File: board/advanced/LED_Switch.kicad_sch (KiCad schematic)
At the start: 14 parts, among them J11 LED, J12 LED, Q2 2SC4213, Q3 2SC4213, SW3 SW_{R}, SW4 SW_{L}, SW5 SW_DIP_x04

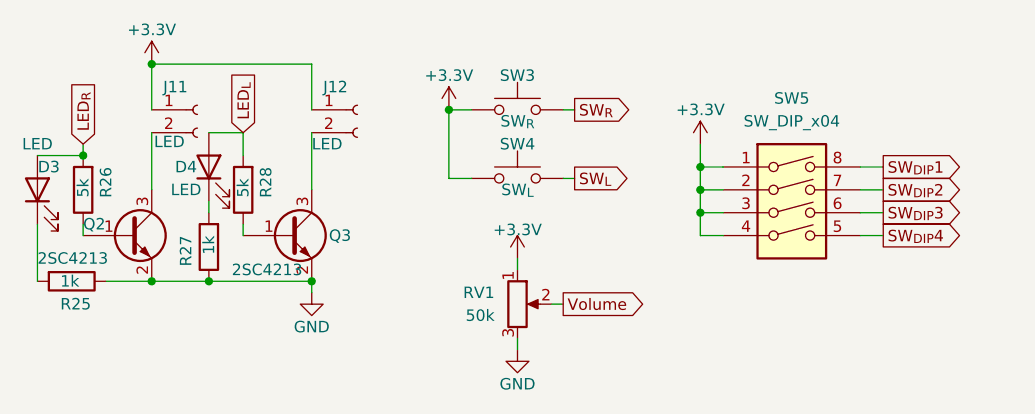
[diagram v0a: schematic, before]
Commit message: put footprints and change schematics
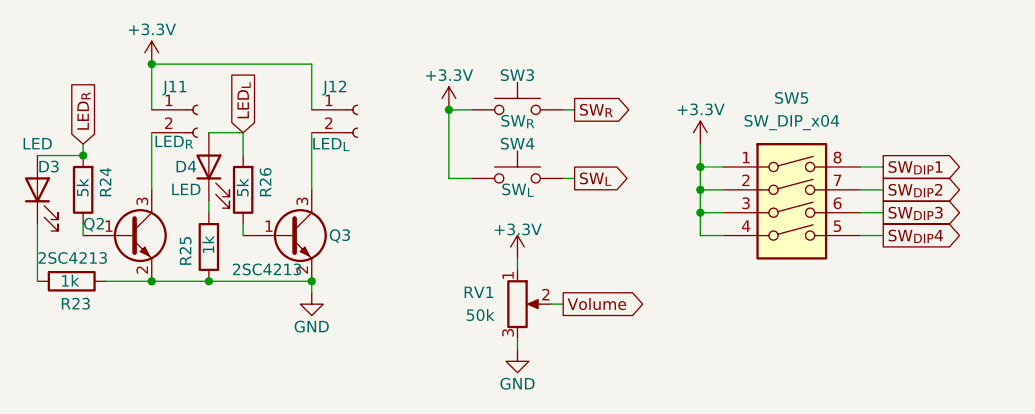
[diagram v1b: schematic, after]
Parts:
- J11: value LED -> LED_{R}
- J12: value LED -> LED_{L}
- R23: renamed from R25; footprint Resistor_SMD:R_0603_1608Metric -> Resistor_SMD:R_0402_1005Metric
- R24: renamed from R26; footprint Resistor_SMD:R_0603_1608Metric -> Resistor_SMD:R_0402_1005Metric
- R25: renamed from R27; footprint Resistor_SMD:R_0603_1608Metric -> Resistor_SMD:R_0402_1005Metric
- R26: renamed from R28; footprint Resistor_SMD:R_0603_1608Metric -> Resistor_SMD:R_0402_1005Metric
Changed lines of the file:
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@@
 		(on_board yes)
 		(dnp no)
-		(property "Reference" "#PWR065"
+		(property "Reference" "#PWR067"
 			(at 160.02 104.14 0)
 			(hide yes)
@@
 			(project "TurtlePico-Minimal"
 				(path "/7af2d99d-e350-48e7-86b4-20911ea922f3/3559871a-0f23-4a86-a659-f5f50e9db57b"
-					(reference "#PWR065")
+					(reference "#PWR067")
 					(unit 1)
 				)
@@
 		(on_board yes)
 		(dnp no)
-		(property "Reference" "#PWR068"
+		(property "Reference" "#PWR070"
 			(at 187.96 107.95 0)
 			(hide yes)
@@
 			(project "TurtlePico-Minimal"
 				(path "/7af2d99d-e350-48e7-86b4-20911ea922f3/3559871a-0f23-4a86-a659-f5f50e9db57b"
-					(reference "#PWR068")
+					(reference "#PWR070")
 					(unit 1)
 				)
@@
 		(on_board yes)
 		(dnp no)
-		(property "Reference" "#PWR067"
+		(property "Reference" "#PWR069"
 			(at 167.64 133.35 0)
 			(hide yes)
@@
 			(project "TurtlePico-Minimal"
 				(path "/7af2d99d-e350-48e7-86b4-20911ea922f3/3559871a-0f23-4a86-a659-f5f50e9db57b"
-					(reference "#PWR067")
+					(reference "#PWR069")
 					(unit 1)
 				)
@@
 		(on_board yes)
 		(dnp no)
-		(property "Reference" "#PWR066"
+		(property "Reference" "#PWR068"
 			(at 167.64 120.65 0)
 			(hide yes)
@@
 			(project "TurtlePico-Minimal"
 				(path "/7af2d99d-e350-48e7-86b4-20911ea922f3/3559871a-0f23-4a86-a659-f5f50e9db57b"
-					(reference "#PWR066")
+					(reference "#PWR068")
 					(unit 1)
 				)
@@
 		(on_board yes)
 		(dnp no)
-		(property "Reference" "R25"
+		(property "Reference" "R23"
 			(at 116.84 121.92 90)
 			(effects
@@
 			)
 		)
-		(property "Footprint" "Resistor_SMD:R_0603_1608Metric"
+		(property "Footprint" "Resistor_SMD:R_0402_1005Metric"
 			(at 118.11 117.602 90)
 			(hide yes)
@@
 			(project "TurtlePico-Minimal"
 				(path "/7af2d99d-e350-48e7-86b4-20911ea922f3/3559871a-0f23-4a86-a659-f5f50e9db57b"
-					(reference "R25")
+					(reference "R23")
 					(unit 1)
 				)
@@
 			)
 		)
-		(property "Value" "LED"
+		(property "Value" "LED_{L}"
 			(at 144.78 104.14 0)
 			(effects
@@
 		(on_board yes)
 		(dnp no)
-		(property "Reference" "R27"
+		(property "Reference" "R25"
 			(at 130.81 114.3 90)
 			(effects
@@
 			)
 		)
-		(property "Footprint" "Resistor_SMD:R_0603_1608Metric"
+		(property "Footprint" "Resistor_SMD:R_0402_1005Metric"
 			(at 135.128 115.57 90)
 			(hide yes)
@@
 			(project "TurtlePico-Minimal"
 				(path "/7af2d99d-e350-48e7-86b4-20911ea922f3/3559871a-0f23-4a86-a659-f5f50e9db57b"
-					(reference "R27")
+					(reference "R25")
 					(unit 1)
 				)
@@
 		(on_board yes)
 		(dnp no)
-		(property "Reference" "R26"
+		(property "Reference" "R24"
 			(at 121.92 106.68 90)
 			(effects
@@
 			)
 		)
-		(property "Footprint" "Resistor_SMD:R_0603_1608Metric"
+		(property "Footprint" "Resistor_SMD:R_0402_1005Metric"
 			(at 121.158 109.22 90)
 			(hide yes)
@@
 			(project "TurtlePico-Minimal"
 				(path "/7af2d99d-e350-48e7-86b4-20911ea922f3/3559871a-0f23-4a86-a659-f5f50e9db57b"
-					(reference "R26")
+					(reference "R24")
 					(unit 1)
 				)
@@
 		(on_board yes)
 		(dnp no)
-		(property "Reference" "#PWR063"
+		(property "Reference" "#PWR065"
 			(at 127 99.06 0)
 			(hide yes)
@@
 			(project "TurtlePico-Minimal"
 				(path "/7af2d99d-e350-48e7-86b4-20911ea922f3/3559871a-0f23-4a86-a659-f5f50e9db57b"
-					(reference "#PWR063")
+					(reference "#PWR065")
 					(unit 1)
 				)
@@
 			)
 		)
-		(property "Value" "LED"
+		(property "Value" "LED_{R}"
 			(at 127.254 103.886 0)
 			(effects
@@
 		(on_board yes)
 		(dnp no)
-		(property "Reference" "#PWR064"
+		(property "Reference" "#PWR066"
 			(at 144.78 127 0)
 			(hide yes)
@@
 			(project "TurtlePico-Minimal"
 				(path "/7af2d99d-e350-48e7-86b4-20911ea922f3/3559871a-0f23-4a86-a659-f5f50e9db57b"
-					(reference "#PWR064")
+					(reference "#PWR066")
 					(unit 1)
 				)
@@
 		(on_board yes)
 		(dnp no)
-		(property "Reference" "R28"
+		(property "Reference" "R26"
 			(at 139.7 106.68 90)
 			(effects
@@
 			)
 		)
-		(property "Footprint" "Resistor_SMD:R_0603_1608Metric"
+		(property "Footprint" "Resistor_SMD:R_0402_1005Metric"
 			(at 138.938 109.22 90)
 			(hide yes)
@@
 			(project "TurtlePico-Minimal"
 				(path "/7af2d99d-e350-48e7-86b4-20911ea922f3/3559871a-0f23-4a86-a659-f5f50e9db57b"
-					(reference "R28")
-					(unit 1)
-				)
+					(reference "R26")
+					(unit 1)
+				)

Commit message: change schematics and complete wiring
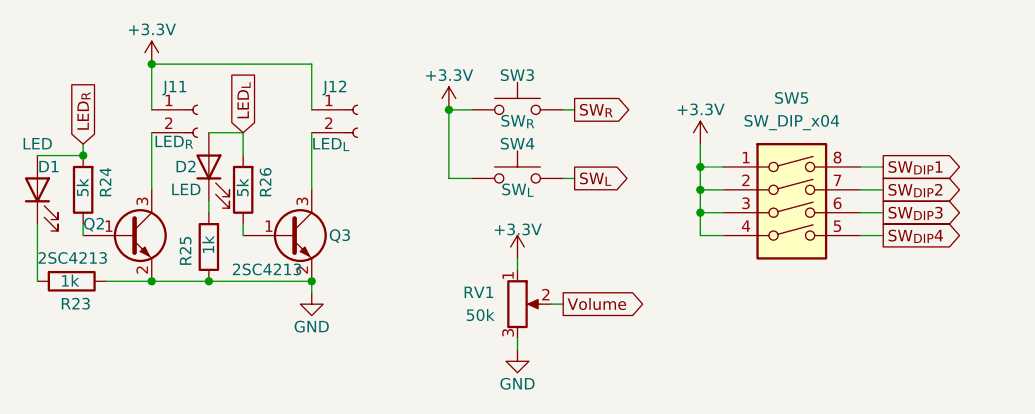
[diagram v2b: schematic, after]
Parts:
- R23, R24, R25, R26: footprint Resistor_SMD:R_0402_1005Metric -> C_0402_1005Metric_small_pads:C_0402_1005Metric_small_pads
- renumbered D3 to D1, D4 to D2
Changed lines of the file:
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@@
 		(on_board yes)
 		(dnp no)
-		(property "Reference" "#PWR067"
+		(property "Reference" "#PWR062"
 			(at 160.02 104.14 0)
 			(hide yes)
@@
 			(project "TurtlePico-Minimal"
 				(path "/7af2d99d-e350-48e7-86b4-20911ea922f3/3559871a-0f23-4a86-a659-f5f50e9db57b"
-					(reference "#PWR067")
+					(reference "#PWR062")
 					(unit 1)
 				)
@@
 		(on_board yes)
 		(dnp no)
-		(property "Reference" "#PWR070"
+		(property "Reference" "#PWR065"
 			(at 187.96 107.95 0)
 			(hide yes)
@@
 			(project "TurtlePico-Minimal"
 				(path "/7af2d99d-e350-48e7-86b4-20911ea922f3/3559871a-0f23-4a86-a659-f5f50e9db57b"
-					(reference "#PWR070")
+					(reference "#PWR065")
 					(unit 1)
 				)
@@
 		(on_board yes)
 		(dnp no)
-		(property "Reference" "#PWR069"
+		(property "Reference" "#PWR064"
 			(at 167.64 133.35 0)
 			(hide yes)
@@
 			(project "TurtlePico-Minimal"
 				(path "/7af2d99d-e350-48e7-86b4-20911ea922f3/3559871a-0f23-4a86-a659-f5f50e9db57b"
-					(reference "#PWR069")
+					(reference "#PWR064")
 					(unit 1)
 				)
@@
 		(on_board yes)
 		(dnp no)
-		(property "Reference" "#PWR068"
+		(property "Reference" "#PWR063"
 			(at 167.64 120.65 0)
 			(hide yes)
@@
 			(project "TurtlePico-Minimal"
 				(path "/7af2d99d-e350-48e7-86b4-20911ea922f3/3559871a-0f23-4a86-a659-f5f50e9db57b"
-					(reference "#PWR068")
+					(reference "#PWR063")
 					(unit 1)
 				)
@@
 			)
 		)
-		(property "Footprint" "Resistor_SMD:R_0402_1005Metric"
+		(property "Footprint" "C_0402_1005Metric_small_pads:C_0402_1005Metric_small_pads"
 			(at 118.11 117.602 90)
 			(hide yes)
@@
 		(on_board yes)
 		(dnp no)
-		(property "Reference" "D3"
+		(property "Reference" "D1"
 			(at 115.57 106.68 90)
 			(effects
@@
 			(project "TurtlePico-Minimal"
 				(path "/7af2d99d-e350-48e7-86b4-20911ea922f3/3559871a-0f23-4a86-a659-f5f50e9db57b"
-					(reference "D3")
+					(reference "D1")
 					(unit 1)
 				)
@@
 			)
 		)
-		(property "Footprint" "Resistor_SMD:R_0402_1005Metric"
+		(property "Footprint" "C_0402_1005Metric_small_pads:C_0402_1005Metric_small_pads"
 			(at 135.128 115.57 90)
 			(hide yes)
@@
 			)
 		)
-		(property "Footprint" "Resistor_SMD:R_0402_1005Metric"
+		(property "Footprint" "C_0402_1005Metric_small_pads:C_0402_1005Metric_small_pads"
 			(at 121.158 109.22 90)
 			(hide yes)
@@
 		(on_board yes)
 		(dnp no)
-		(property "Reference" "#PWR065"
+		(property "Reference" "#PWR060"
 			(at 127 99.06 0)
 			(hide yes)
@@
 			(project "TurtlePico-Minimal"
 				(path "/7af2d99d-e350-48e7-86b4-20911ea922f3/3559871a-0f23-4a86-a659-f5f50e9db57b"
-					(reference "#PWR065")
+					(reference "#PWR060")
 					(unit 1)
 				)
@@
 		(on_board yes)
 		(dnp no)
-		(property "Reference" "#PWR066"
+		(property "Reference" "#PWR061"
 			(at 144.78 127 0)
 			(hide yes)
@@
 			(project "TurtlePico-Minimal"
 				(path "/7af2d99d-e350-48e7-86b4-20911ea922f3/3559871a-0f23-4a86-a659-f5f50e9db57b"
-					(reference "#PWR066")
+					(reference "#PWR061")
 					(unit 1)
 				)
@@
 			)
 		)
-		(property "Footprint" "Resistor_SMD:R_0402_1005Metric"
+		(property "Footprint" "C_0402_1005Metric_small_pads:C_0402_1005Metric_small_pads"
 			(at 138.938 109.22 90)
 			(hide yes)
@@
 		(on_board yes)
 		(dnp no)
-		(property "Reference" "D4"
+		(property "Reference" "D2"
 			(at 130.81 106.68 90)
 			(effects
@@
 			(project "TurtlePico-Minimal"
 				(path "/7af2d99d-e350-48e7-86b4-20911ea922f3/3559871a-0f23-4a86-a659-f5f50e9db57b"
-					(reference "D4")
-					(unit 1)
-				)
+					(reference "D2")
+					(unit 1)
+				)

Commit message: add LTB example and more
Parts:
- D1: Mouser Part Number (none) -> 755-SML-D12V8WT86; Mouser Price/Stock (none) -> https://www.mouser.jp/ProductDetail/ROHM-Semiconductor/SML-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
- D2: Mouser Part Number (none) -> 755-SML-D12M8WT86; Mouser Price/Stock (none) -> https://www.mouser.jp/ProductDetail/ROHM-Semiconductor/SML-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
- Q2, Q3: Mouser Price/Stock https://www.mouser.jp/ProductDetail/757-2SC4213-ATE85LF -> https://www.mouser.jp/ProductDetail/Toshiba/2SC4213-ATE85LF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
- R23, R25: Mouser Part Number 660-RN73H1JT5102F100 -> 667-ERJ-2GEJ102X; Mouser Price/Stock https://www.mouser.jp/ProductDetail/660-RN73H1JT5102F100 -> https://www.mouser.jp/ProductDetail/Panasonic/ERJ-2GEJ102X?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
- R24, R26: value 5k -> 4.7k; Mouser Part Number 660-RN73H1JT5102F100 -> 667-ERJ-2RKF4701X; Mouser Price/Stock https://www.mouser.jp/ProductDetail/660-RN73H1JT5102F100 -> https://www.mouser.jp/ProductDetail/Panasonic/ERJ-2RKF4701X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
- SW3, SW4: Mouser Part Number (none) -> 688-SKRPACE010; Mouser Price/Stock (none) -> https://www.mouser.jp/ProductDetail/Alps-Alpine/SKRPACE010?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
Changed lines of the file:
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@@
 			)
 		)
-		(property "Mouser Price/Stock" "https://www.mouser.jp/ProductDetail/757-2SC4213-ATE85LF"
+		(property "Mouser Price/Stock" "https://www.mouser.jp/ProductDetail/Toshiba/2SC4213-ATE85LF?qs=vnMp2KDihub2h7dVJUge2w%3D%3D"
 			(at 142.24 114.3 0)
 			(hide yes)
@@
 			)
 		)
-		(property "Mouser Price/Stock" "https://www.mouser.jp/ProductDetail/757-2SC4213-ATE85LF"
+		(property "Mouser Price/Stock" "https://www.mouser.jp/ProductDetail/Toshiba/2SC4213-ATE85LF?qs=vnMp2KDihub2h7dVJUge2w%3D%3D"
 			(at 124.46 114.3 0)
 			(hide yes)
@@
 			)
 		)
-		(property "Mouser Part Number" "660-RN73H1JT5102F100"
+		(property "Mouser Part Number" "667-ERJ-2GEJ102X"
 			(at 118.11 119.38 0)
 			(hide yes)
@@
 			)
 		)
-		(property "Mouser Price/Stock" "https://www.mouser.jp/ProductDetail/660-RN73H1JT5102F100"
+		(property "Mouser Price/Stock" "https://www.mouser.jp/ProductDetail/Panasonic/ERJ-2GEJ102X?qs=sGAEpiMZZMtG0KNrPCHnjSOOg5ypiLdnrFEbXWcegG4%3D"
 			(at 118.11 119.38 0)
 			(hide yes)
@@
 			)
 		)
+		(property "Mouser Part Number" "755-SML-D12V8WT86"
+			(at 114.3 109.22 90)
+			(hide yes)
+			(effects
+				(font
+					(size 1.27 1.27)
+				)
+			)
+		)
+		(property "Mouser Price/Stock" "https://www.mouser.jp/ProductDetail/ROHM-Semiconductor/SML-D12V8WT86?qs=sGAEpiMZZMvVL5Kk7ZYykVdSwGyztViF8nbP2%252BAo1so%3D"
+			(at 114.3 109.22 90)
+			(hide yes)
+			(effects
+				(font
+					(size 1.27 1.27)
+				)
+			)
+		)
 		(pin "2"
 		)
@@
 			)
 		)
+		(property "Mouser Part Number" "688-SKRPACE010"
+			(at 167.64 107.95 0)
+			(hide yes)
+			(effects
+				(font
+					(size 1.27 1.27)
+				)
+			)
+		)
+		(property "Mouser Price/Stock" "https://www.mouser.jp/ProductDetail/Alps-Alpine/SKRPACE010?qs=dHDuPHwQO79W8iY66hDbLQ%3D%3D"
+			(at 167.64 107.95 0)
+			(hide yes)
+			(effects
+				(font
+					(size 1.27 1.27)
+				)
+			)
+		)
 		(pin "2"
 		)
@@
 			)
 		)
-		(property "Mouser Part Number" "660-RN73H1JT5102F100"
+		(property "Mouser Part Number" "667-ERJ-2GEJ102X"
 			(at 133.35 115.57 0)
 			(hide yes)
@@
 			)
 		)
-		(property "Mouser Price/Stock" "https://www.mouser.jp/ProductDetail/660-RN73H1JT5102F100"
+		(property "Mouser Price/Stock" "https://www.mouser.jp/ProductDetail/Panasonic/ERJ-2GEJ102X?qs=sGAEpiMZZMtG0KNrPCHnjSOOg5ypiLdnrFEbXWcegG4%3D"
 			(at 133.35 115.57 0)
 			(hide yes)
@@
 			)
 		)
+		(property "Mouser Part Number" "688-SKRPACE010"
+			(at 167.64 100.33 0)
+			(hide yes)
+			(effects
+				(font
+					(size 1.27 1.27)
+				)
+			)
+		)
+		(property "Mouser Price/Stock" "https://www.mouser.jp/ProductDetail/Alps-Alpine/SKRPACE010?qs=dHDuPHwQO79W8iY66hDbLQ%3D%3D"
+			(at 167.64 100.33 0)
+			(hide yes)
+			(effects
+				(font
+					(size 1.27 1.27)
+				)
+			)
+		)
 		(pin "2"
 		)
@@
 			)
 		)
-		(property "Value" "5k"
+		(property "Value" "4.7k"
 			(at 119.38 107.95 90)
 			(effects
@@
 			)
 		)
-		(property "Mouser Part Number" "660-RN73H1JT5102F100"
+		(property "Mouser Part Number" "667-ERJ-2RKF4701X"
 			(at 119.38 109.22 0)
 			(hide yes)
@@
 			)
 		)
-		(property "Mouser Price/Stock" "https://www.mouser.jp/ProductDetail/660-RN73H1JT5102F100"
+		(property "Mouser Price/Stock" "https://www.mouser.jp/ProductDetail/Panasonic/ERJ-2RKF4701X?qs=sGAEpiMZZMtG0KNrPCHnjWXb3yLuGJ27W1oy%252BMcLHTs%3D"
 			(at 119.38 109.22 0)
 			(hide yes)
@@
 			)
 		)
-		(property "Value" "5k"
+		(property "Value" "4.7k"
 			(at 137.16 107.95 90)
 			(effects
@@
 			)
 		)
-		(property "Mouser Part Number" "660-RN73H1JT5102F100"
+		(property "Mouser Part Number" "667-ERJ-2RKF4701X"
 			(at 137.16 109.22 0)
 			(hide yes)
@@
 			)
 		)
-		(property "Mouser Price/Stock" "https://www.mouser.jp/ProductDetail/660-RN73H1JT5102F100"
+		(property "Mouser Price/Stock" "https://www.mouser.jp/ProductDetail/Panasonic/ERJ-2RKF4701X?qs=sGAEpiMZZMtG0KNrPCHnjWXb3yLuGJ27W1oy%252BMcLHTs%3D"
 			(at 137.16 109.22 0)
 			(hide yes)
@@
 			(effects
 				(font
+					(size 1.27 1.27)
+				)
+			)
+		)
+		(property "Mouser Part Number" "755-SML-D12M8WT86"
+			(at 133.35 106.68 90)
+			(hide yes)
+			(effects
+				(font
+					(size 1.27 1.27)
+				)
+			)
+		)
+		(property "Mouser Price/Stock" "https://www.mouser.jp/ProductDetail/ROHM-Semiconductor/SML-D12M8WT86?qs=sGAEpiMZZMvVL5Kk7ZYykVdSwGyztViFSeegmzgd8%2FM%3D"
+			(at 133.35 106.68 90)
+			(hide yes)
+			(effects
+				(font
